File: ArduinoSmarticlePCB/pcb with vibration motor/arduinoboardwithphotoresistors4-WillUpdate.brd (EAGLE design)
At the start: 48.8 x 17.4 mm, 23 parts, among them Q1 200mA/40V

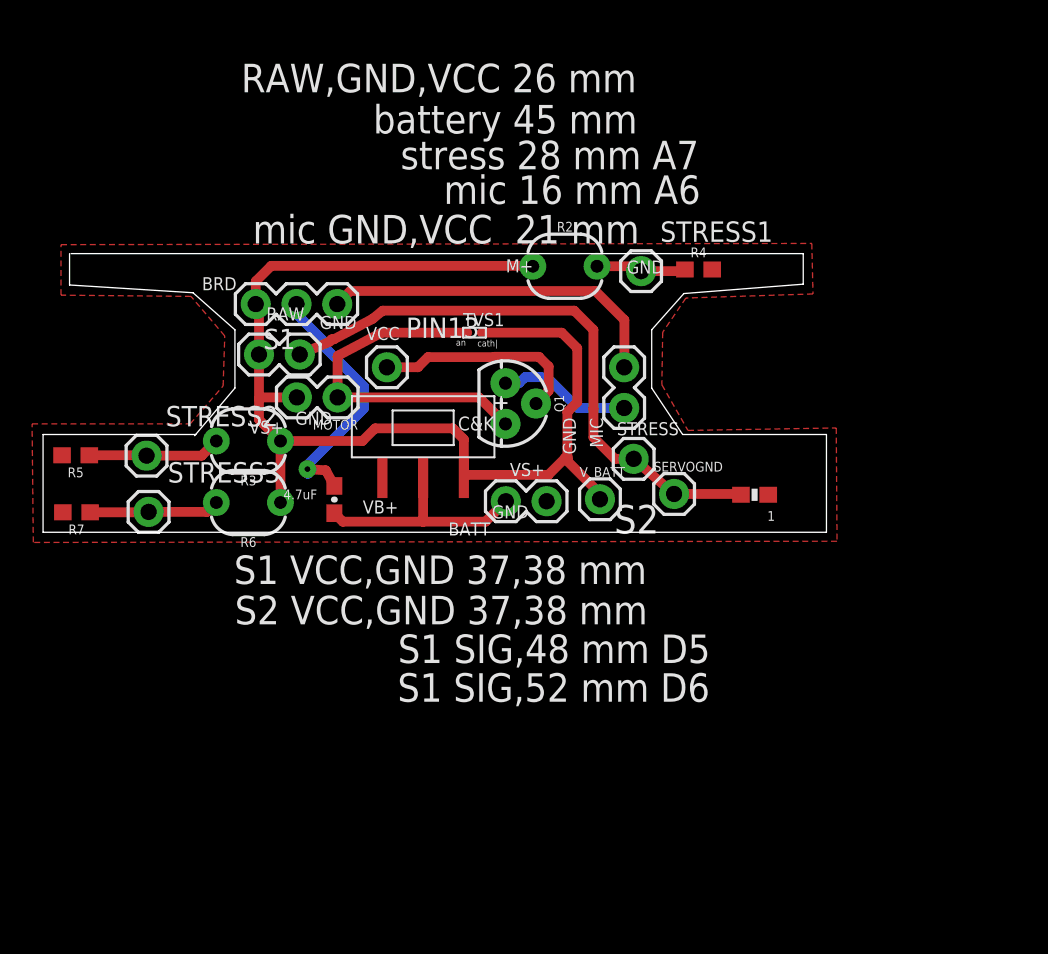
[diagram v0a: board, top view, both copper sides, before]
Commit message: added text for new lengths and fixed diode
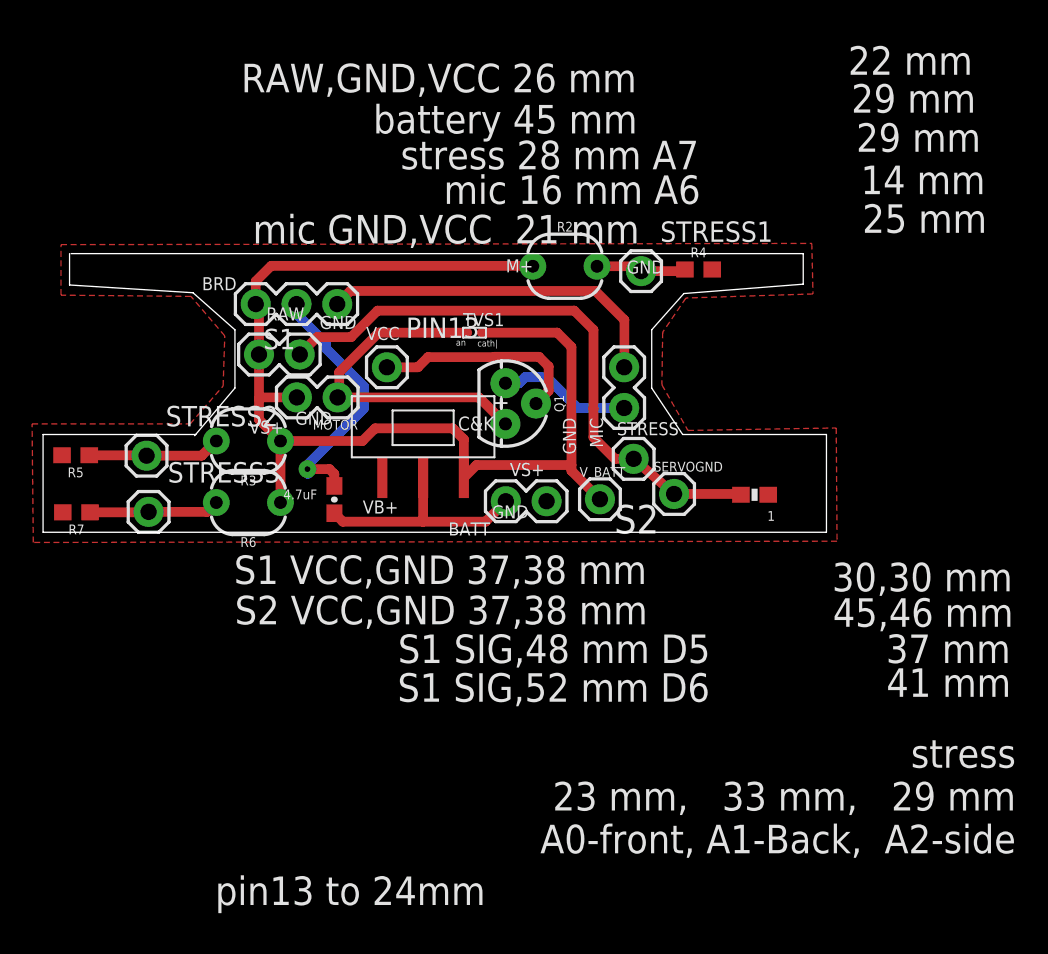
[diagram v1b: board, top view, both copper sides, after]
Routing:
- net V_BATT: track 73.0 -> 72.2 mm
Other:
- board text added: "14 mm"
- board text added: "22 mm"
- board text added: "25 mm"
- board text added: "29 mm"
- board text added: "30,30 mm"
- board text added: "37 mm"
- board text added: "41 mm"
- board text added: "45,46 mm"
- board text added: "pin13 to 24mm"
- board text added: "stress 23 mm, 33 mm, 29 mm A0-front, A1-Back, A2-side"
